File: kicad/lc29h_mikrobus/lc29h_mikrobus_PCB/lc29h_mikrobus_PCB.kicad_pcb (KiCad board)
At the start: 2 copper layers, 27.4 x 30.7 mm, 4 parts, among them IC1 MIKROE-924

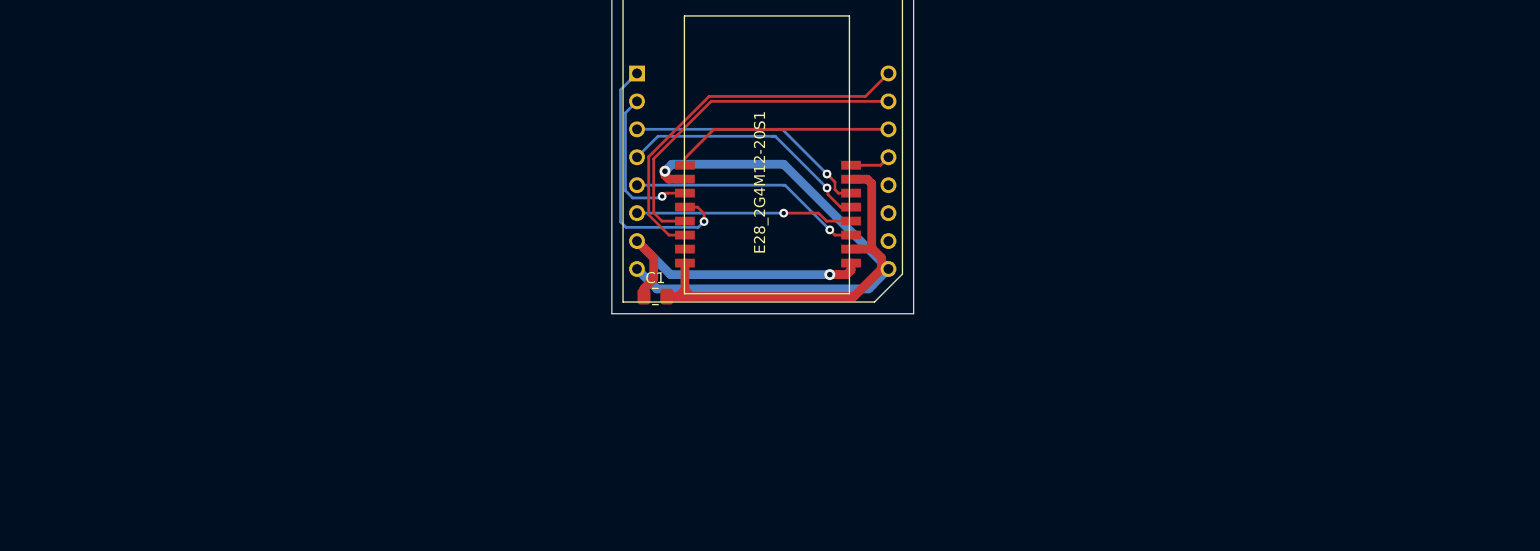
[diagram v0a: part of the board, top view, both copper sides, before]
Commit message: Ajout symboles/empreintes composants
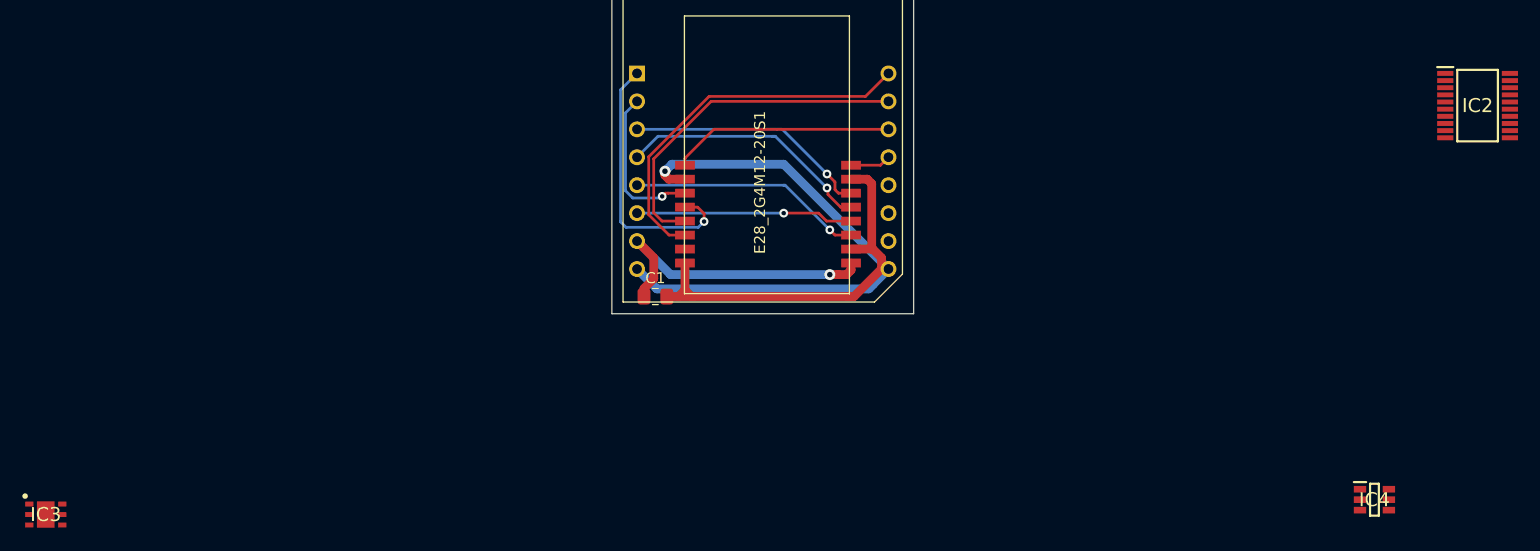
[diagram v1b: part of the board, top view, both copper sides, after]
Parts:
- added IC2: TXS0108EPWR, TXS0108EPWR:SOP65P640X120-20N, F.Cu at (202.5, 78.1)
- added IC3: DS28E36BQ+U, DS28E36BQ+U:SON95P300X300X80-7N, F.Cu at (72.3, 115.3)
- added IC4: 74LVC1G3157GV,125, 74LVC1G3157GV_125:SOP95P275X110-6N, F.Cu at (193.1, 114.0)
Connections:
- IC1 pad 13: Net-(IC1-Pad13) -> unconnected-(IC1-SCL-Pad13)
- IC1 pad 14: Net-(IC1-Pad14) -> unconnected-(IC1-SDA-Pad14)
- IC1 pad 15: Net-(IC1-Pad15) -> unconnected-(IC1-+5V-Pad15)

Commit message: Début circuit
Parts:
- removed IC2: TXS0108EPWR, TXS0108EPWR:SOP65P640X120-20N
- removed IC3: DS28E36BQ+U, DS28E36BQ+U:SON95P300X300X80-7N
- removed IC4: 74LVC1G3157GV,125, 74LVC1G3157GV_125:SOP95P275X110-6N

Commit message: Ajout empreinte PCB
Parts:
- removed C1: 100nF, Capacitor_SMD:C_0805_2012Metric_Pad1.18x1.45mm_HandSolder
- removed E28_2G4M12-20S1: E28, LIB_E28-2G4M12-20S:E28-2G4M12-20S
- added BT101: 3000TR, 3000TR:3000TR, F.Cu at (247.2, 55.4)
- added D102: ESDARF02-1BU2CK, ESDARF02-1BU2CK:ESDARF021BU2CK, F.Cu at (251.4, 72.7)
- added IC101: DS28E36BQ+U, DS28E36BQ+U:SON95P300X300X80-7N, F.Cu at (173.6, 54.2)
- added IC102: 74LVC1G3157GV,125, 74LVC1G3157GV_125:SOP95P275X110-6N, F.Cu at (192.8, 91.8)
- added IC103: TXS0102DQER, TXS0102DQER:SON35P100X140X40-8N, F.Cu at (196.6, 81.7)
- added Q1: DMP3013SFV, Package_SON:Diodes_PowerDI3333-8, F.Cu at (155.1, 38.7)
- added Q101: BC856B-13-F, BC856B-13-F:SOT96P240X110-3N, F.Cu at (174.0, 59.7)
- added Q102: BSS123L, BSS123L:SOT96P237X111-3N, F.Cu at (175.1, 46.3)
- added SW101: SW_Nidec_CAS-120A1, Button_Switch_SMD:Nidec_Copal_CAS-120A, F.Cu at (175.2, 68.5)
- added U101: LC29H, LC29H:LC29HEA, F.Cu at (227.1, 94.7)
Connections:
- IC1 pad 1: BUSY -> unconnected-(IC1-AN-Pad1)
- IC1 pad 10: DIO1 -> 1PPS
- IC1 pad 11: TXEN -> TX1
- IC1 pad 12: RXEN -> RX1
- IC1 pad 13: unconnected-(IC1-SCL-Pad13) -> SCL
- IC1 pad 14: unconnected-(IC1-SDA-Pad14) -> SDA
- IC1 pad 2: RESET -> RST
- IC1 pad 3: NSS -> CE_HOST
- IC1 pad 4: SCK -> unconnected-(IC1-SCK-Pad4)
- IC1 pad 5: MISO -> unconnected-(IC1-MISO-Pad5)
- IC1 pad 6: MOSI -> unconnected-(IC1-MOSI-Pad6)
- IC1 pad 9: DIO2 -> WUP
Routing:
- net GND: track 89.3 -> 0.00 mm, vias 1 -> 0
- net DIO2: track 34.3 -> 0.00 mm
- net DIO1: track 31.6 -> 0.00 mm
- net VCC: track 27.6 -> 0.00 mm, vias 1 -> 0
- net BUSY: track 24.8 -> 0.00 mm, vias 1 -> 0
- net SCK: track 23.4 -> 0.00 mm, vias 1 -> 0
- net NSS: track 22.3 -> 0.00 mm, vias 1 -> 0
- net MISO: track 21.3 -> 0.00 mm, vias 1 -> 0
- net TXEN: track 20.2 -> 0.00 mm
- net MOSI: track 19.8 -> 0.00 mm, vias 1 -> 0
- net RESET: track 14.4 -> 0.00 mm, vias 1 -> 0
- net RXEN: track 3.70 -> 0.00 mm
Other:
- board size 27.4 x 30.7 mm -> 27.4 x 66.3 mm
- board text added: "Mikrobus gnss_rtk_3_click"
- board text removed: "Mikrobus E28-2G4M12/20S"

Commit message: debut connexion pcb
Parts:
- BT101: moved to B.Cu
- moved D102 126.7 mm to (129.3, 38.7)
- moved BT101 109.2 mm to (138.1, 58.2), turned to 180 degrees
- moved U101 96.2 mm to (138.1, 58.2), turned to -90 degrees
- moved IC102 61.8 mm to (132.8, 76.8), turned to 180 degrees
- moved IC103 57.7 mm to (138.9, 80.1), turned to -90 degrees
- moved Q102 54.7 mm to (133.1, 81.3), turned to 90 degrees
- moved IC101 51.3 mm to (133.1, 85.7), turned to -90 degrees
- moved Q101 38.1 mm to (137.1, 69.0), turned to 90 degrees
- moved SW101 35.5 mm to (147.6, 46.2), turned to 180 degrees
- moved Q1 20.3 mm to (134.9, 37.7)
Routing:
- net GND: track 0.00 -> 32.7 mm
- net 1PPS: track 0.00 -> 28.2 mm
- net TX1: track 0.00 -> 26.2 mm
- net WUP: track 0.00 -> 24.7 mm
- net RX1: track 0.00 -> 21.5 mm
- net Net-(Q101-C): track 0.00 -> 16.5 mm
- net VCC: track 0.00 -> 12.0 mm
- net Net-(SW101-B): track 0.00 -> 10.8 mm
- net Net-(IC102-Y0): track 0.00 -> 5.31 mm
- net Net-(IC101-IO): track 0.00 -> 2.30 mm
- net RST: track 0.00 -> 1.38 mm

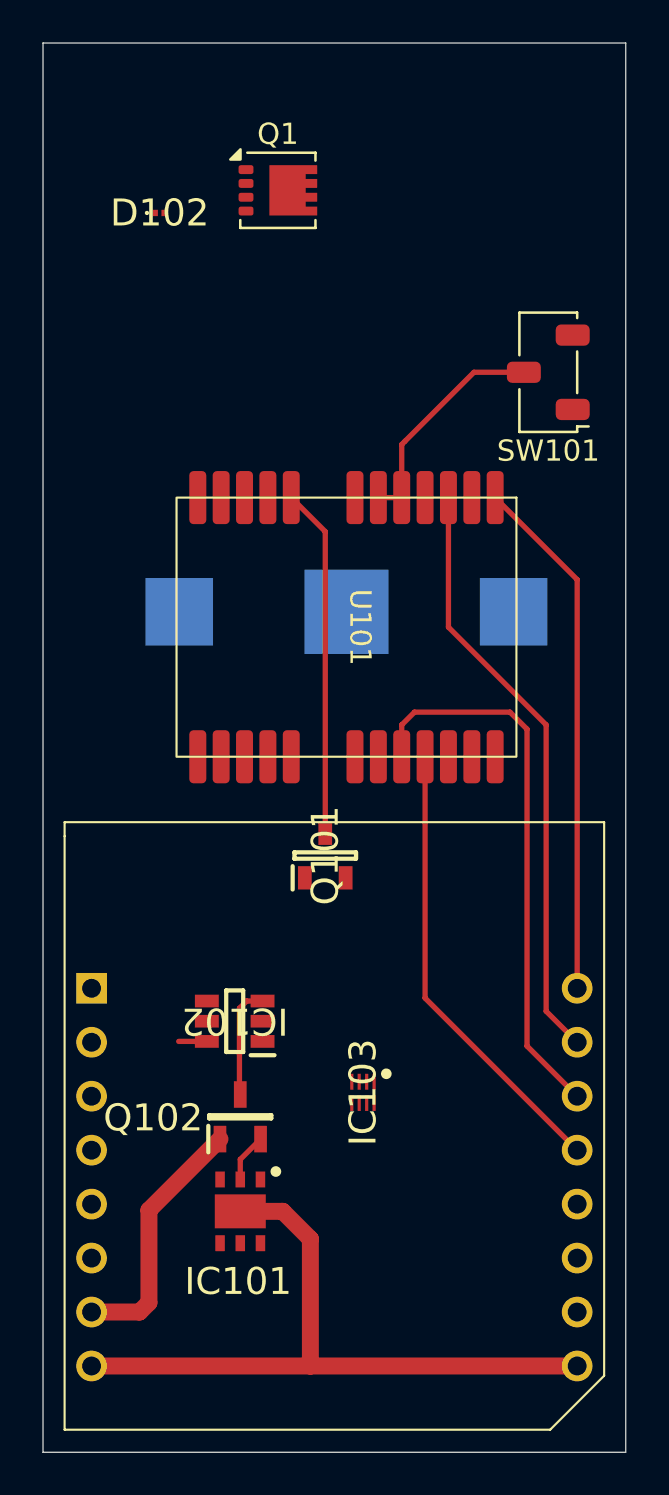
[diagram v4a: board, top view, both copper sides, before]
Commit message: Connexion PCB Composant et alimentation
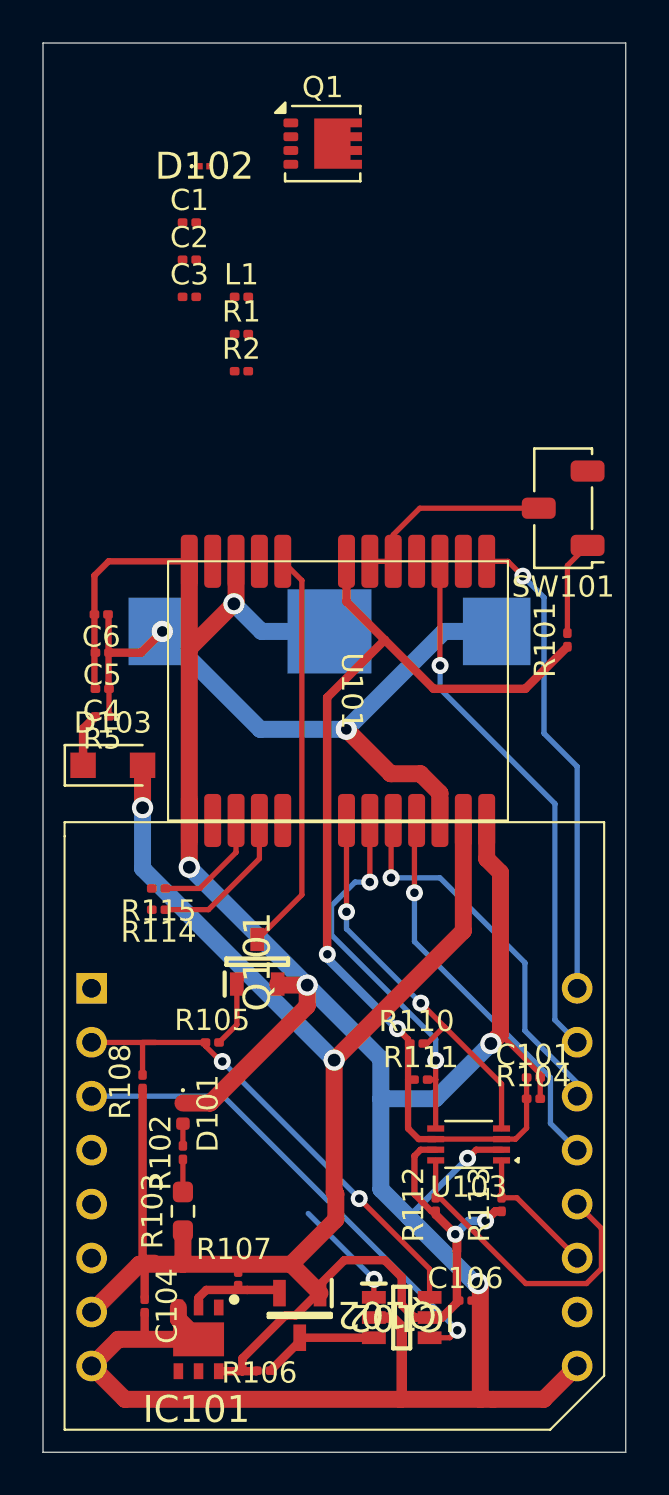
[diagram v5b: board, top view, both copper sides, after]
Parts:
- removed BT101: 3000TR, 3000TR:3000TR
- removed IC103: TXS0102DQER, TXS0102DQER:SON35P100X140X40-8N
- added BT1: 3000TR, 3000TR:3000TR, B.Cu at (137.3, 59.1)
- added C1: 100p, Capacitor_SMD:C_0201_0603Metric, F.Cu at (130.7, 39.2)
- added C101: 100n, Capacitor_SMD:C_0201_0603Metric, F.Cu at (146.9, 79.4)
- added C104: 0.47u, Capacitor_SMD:C_0201_0603Metric, F.Cu at (128.6, 90.2)
- added C106: 100n, Capacitor_SMD:C_0201_0603Metric, F.Cu at (143.7, 89.9)
- added C2: 100n, Capacitor_SMD:C_0201_0603Metric, F.Cu at (130.7, 40.9)
- added C3: 100p, Capacitor_SMD:C_0201_0603Metric, F.Cu at (130.7, 42.7)
- added C4: 33p, Capacitor_SMD:C_0201_0603Metric, F.Cu at (126.6, 61.1)
- added C5: 100n, Capacitor_SMD:C_0201_0603Metric, F.Cu at (126.6, 59.4)
- added C6: 4.7u, Capacitor_SMD:C_0201_0603Metric, F.Cu at (126.5, 57.6)
- added D101: LED, LED_SMD:LED_0402_1005Metric, F.Cu at (130.4, 81.1)
- added D103: PMEG3010ER, Diode_SMD:Nexperia_CFP3_SOD-123W, F.Cu at (127.1, 64.7)
- added L1: 68n, Inductor_SMD:L_0201_0603Metric, F.Cu at (133.1, 42.7)
- added R1: 10, Resistor_SMD:R_0201_0603Metric, F.Cu at (133.1, 44.4)
- added R101: 39k, Resistor_SMD:R_0201_0603Metric, F.Cu at (148.5, 58.8)
- added R102: 470, Resistor_SMD:R_0201_0603Metric, F.Cu at (130.4, 83.0)
- added R103: 0, Resistor_SMD:R_0603_1608Metric_Pad0.98x0.95mm_HandSolder, F.Cu at (130.4, 85.7)
- added R104: 120k, Resistor_SMD:R_0201_0603Metric, F.Cu at (146.9, 80.4)
- added R105: 2.2k, Resistor_SMD:R_0201_0603Metric, F.Cu at (131.8, 77.8)
- added R106: 3.3k, Resistor_SMD:R_0201_0603Metric, F.Cu at (134.2, 93.2)
- added R107: 1k, Resistor_SMD:R_0201_0603Metric, F.Cu at (133.0, 88.9)
- added R108: 10k, Resistor_SMD:R_0201_0603Metric, F.Cu at (128.5, 79.6)
- added R110: 4.7k, Resistor_SMD:R_0201_0603Metric, F.Cu at (141.4, 77.8)
- added R111: 4.7k, Resistor_SMD:R_0201_0603Metric, F.Cu at (141.6, 79.5)
- added R112: 4.7k, Resistor_SMD:R_0201_0603Metric, F.Cu at (142.3, 85.4)
- added R113: 4.7k, Resistor_SMD:R_0201_0603Metric, F.Cu at (145.4, 85.4)
- added R114: 1k, Resistor_SMD:R_0201_0603Metric, F.Cu at (129.2, 71.5)
- added R115: 1k, Resistor_SMD:R_0201_0603Metric, F.Cu at (129.2, 70.5)
- added R2: 10k, Resistor_SMD:R_0201_0603Metric, F.Cu at (133.1, 46.2)
- added R5: 1k, Resistor_SMD:R_0201_0603Metric, F.Cu at (126.6, 62.4)
- added U103: TXS0102DCU, Package_SO:VSSOP-8_2.3x2mm_P0.5mm, F.Cu at (143.8, 82.6)
- moved IC102 16.0 mm to (140.7, 90.7), turned to 0 degrees
- moved Q102 9.76 mm to (135.9, 90.6), turned to -90 degrees
- moved SW101 6.44 mm to (148.3, 52.6)
- moved IC101 6.34 mm to (131.1, 91.7)
- moved Q101 5.94 mm to (133.9, 74.0)
- moved Q1 3.05 mm to (137.0, 35.5)
- moved D102 3.05 mm to (131.4, 36.5)
- moved U101 3.03 mm to (137.7, 61.2)
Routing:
- net GND: track 32.7 -> 139.9 mm, vias 0 -> 6
- net VCC: track 12.0 -> 95.5 mm, vias 0 -> 4
- net VDD_EXT: track 0.00 -> 49.2 mm, vias 0 -> 2
- net VBCK: track 0.00 -> 34.0 mm, vias 0 -> 2
- net CE_HOST: track 0.00 -> 23.2 mm, vias 0 -> 1
- net RST: track 1.38 -> 23.9 mm, vias 0 -> 2
- net mSDA: track 0.00 -> 19.0 mm, vias 0 -> 2
- net mSCL: track 0.00 -> 18.1 mm, vias 0 -> 2
- net SCL: track 0.00 -> 15.0 mm
- net TX1: track 26.2 -> 18.0 mm, vias 0 -> 1
- net Net-(U101-RXD2): track 0.00 -> 7.22 mm
- net SDA: track 0.00 -> 6.50 mm
- net Net-(U101-TXD2): track 0.00 -> 5.53 mm
- net CE: track 0.00 -> 5.24 mm, vias 0 -> 1
- net Net-(SW101-C): track 0.00 -> 4.52 mm
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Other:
- board text removed: "SCL"
- board text removed: "TX"

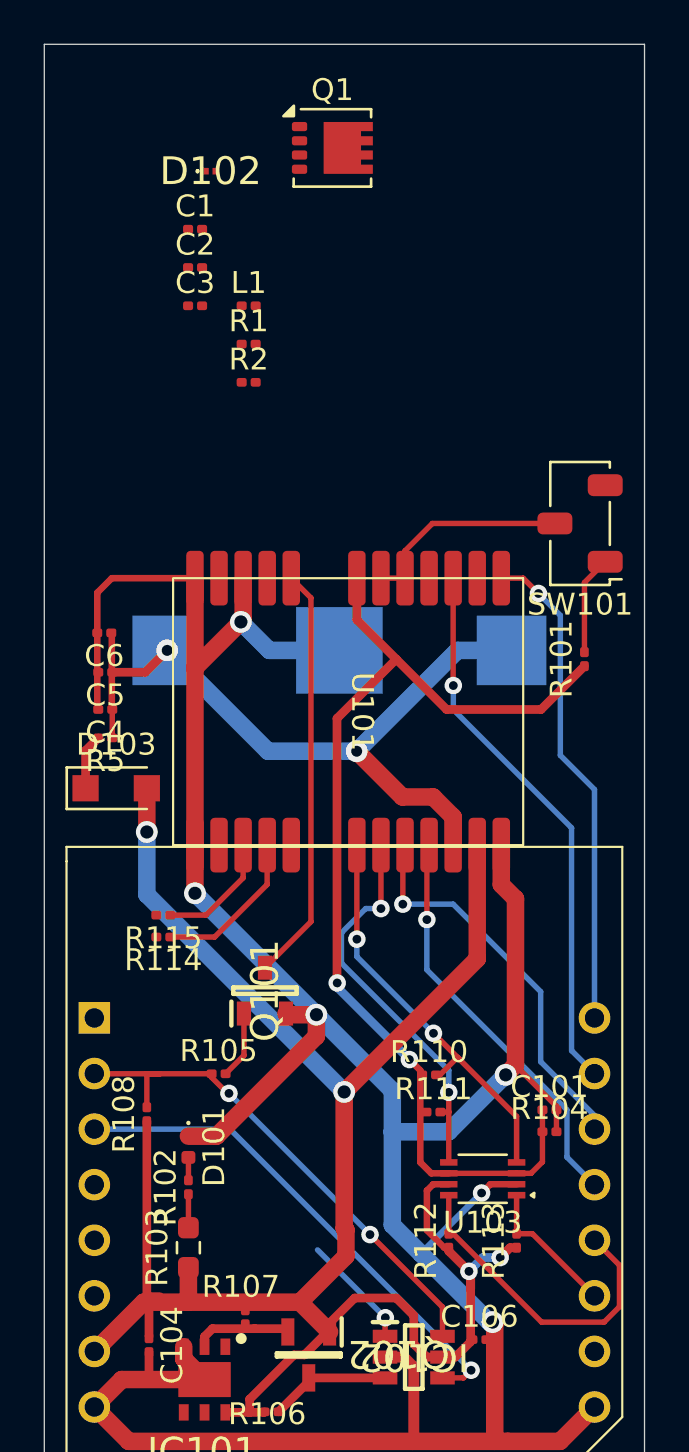
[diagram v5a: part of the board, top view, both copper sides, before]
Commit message: association de toutes les empreintes et début de la finalisation du routage
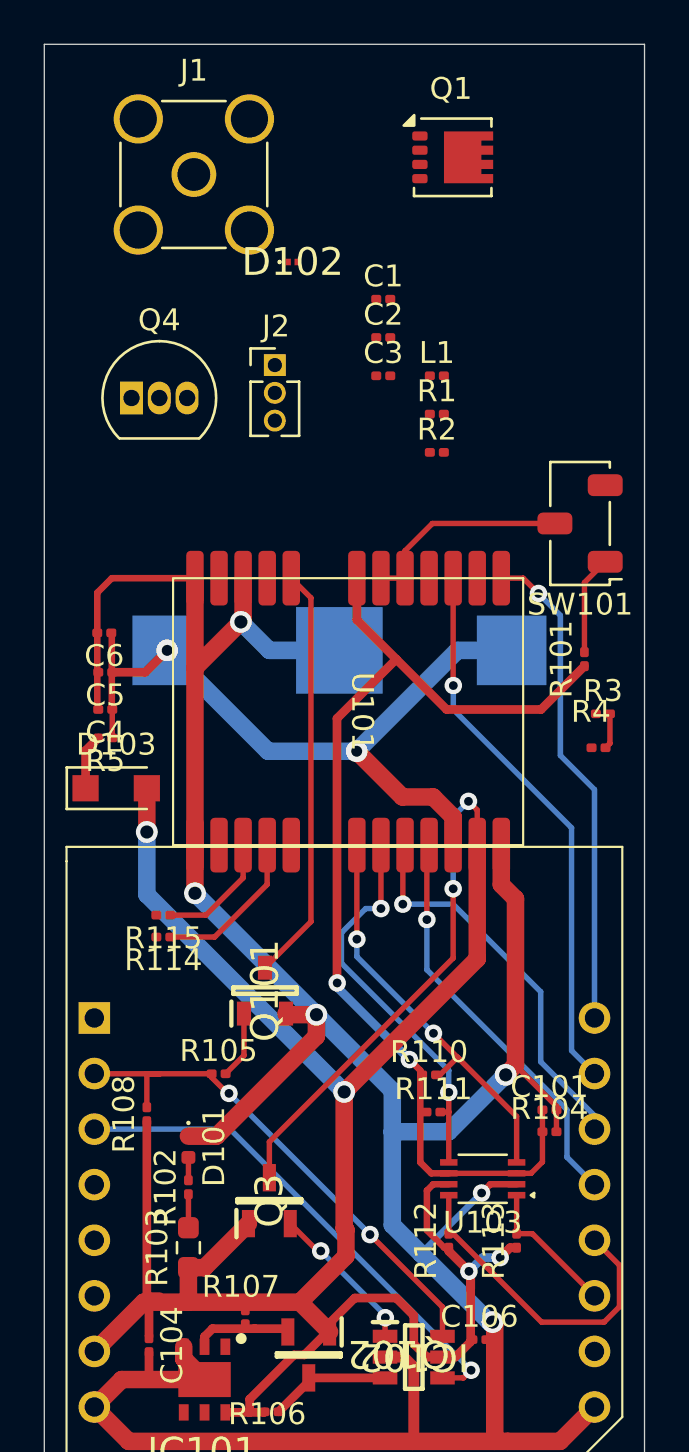
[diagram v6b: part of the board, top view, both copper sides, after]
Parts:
- added J1: Conn_Coaxial, Connector_Coaxial:SMA_Amphenol_901-144_Vertical, F.Cu at (130.6, 36.7)
- added J2: Conn_01x03_Pin, Connector_PinHeader_1.27mm:PinHeader_1x03_P1.27mm_Vertical, F.Cu at (134.3, 45.4)
- added Q3: BSS123L, BSS123L:SOT96P237X111-3N, F.Cu at (134.1, 83.6)
- added Q4: PN2222A, Package_TO_SOT_THT:TO-92_Inline, F.Cu at (127.8, 46.9)
- added R3: 20k, Resistor_SMD:R_0201_0603Metric, F.Cu at (149.3, 61.3)
- added R4: 2k, Resistor_SMD:R_0201_0603Metric, F.Cu at (149.1, 62.9)
- moved C1 9.18 mm to (139.3, 42.4)
- moved C2 9.18 mm to (139.3, 44.1)
- moved C3 9.18 mm to (139.3, 45.9)
- moved L1 9.18 mm to (141.7, 45.9)
- moved R1 9.18 mm to (141.7, 47.6)
- moved R2 9.18 mm to (141.7, 49.4)
- moved D102 5.59 mm to (135.2, 40.7)
- moved Q1 5.52 mm to (142.5, 35.9)
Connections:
- U101 pad 23: VCC -> Net-(Q3-D)
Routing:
- net Net-(Q3-D): track 0.00 -> 22.4 mm, vias 0 -> 2
- net VCC: track 95.5 -> 99.1 mm
- net CE: track 5.24 -> 7.04 mm, vias 1 -> 2
- net Net-(Q4-B): track 0.00 -> 1.63 mm

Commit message: routage carte terminé
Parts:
- moved R3 25.8 mm to (126.2, 50.0)
- moved R4 25.8 mm to (126.2, 51.1), turned to 0 degrees
- moved Q4 16.5 mm to (143.8, 42.7), turned to 180 degrees
- moved J2 13.8 mm to (148.0, 43.7)
- moved Q1 13.2 mm to (142.1, 49.1)
- moved C1 12.8 mm to (131.7, 52.7), turned to -90 degrees
- moved L1 11.2 mm to (132.1, 51.4), turned to 180 degrees
- moved D102 10.2 mm to (131.5, 50.2)
- moved C2 8.62 mm to (133.5, 50.5), turned to 90 degrees
- moved J1 8.35 mm to (131.7, 45.0)
- moved C3 5.92 mm to (135.6, 50.5), turned to 90 degrees
- moved R1 5.52 mm to (137.3, 50.8), turned to 180 degrees
- moved R2 4.20 mm to (137.7, 48.3)
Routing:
- net GND: track 139.9 -> 197.3 mm, vias 6 -> 8
- net Net-(J2-Pin_2): track 0.00 -> 45.2 mm
- net Net-(J2-Pin_3): track 0.00 -> 40.9 mm, vias 0 -> 2
- net Net-(Q4-B): track 1.63 -> 28.4 mm
- net ANT_ON: track 0.00 -> 20.6 mm, vias 0 -> 2
- net VDD_RF: track 0.00 -> 17.8 mm, vias 0 -> 2
- net VCC: track 99.1 -> 85.3 mm
- net Net-(Q1-G): track 0.00 -> 10.3 mm
- net Net-(J1-In): track 0.00 -> 7.42 mm
- net Net-(Q1-D): track 0.00 -> 7.23 mm
- net Net-(C2-Pad1): track 0.00 -> 4.79 mm
- net Net-(Q3-D): track 22.4 -> 19.1 mm, vias 2 -> 0
- net RF_IN: track 0.00 -> 2.23 mm
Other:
- board size 27.4 x 66.3 mm -> 27.4 x 57.5 mm
